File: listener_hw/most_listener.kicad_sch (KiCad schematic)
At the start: 121 parts, among them J1 1-1394640-1, J2 ANALYSER, J3 I2S, J4 VBAT_IN, J5 PLR135/T10, J6 PLT133/T10W, J7 RCA 75R, M1 Tang Nano 20K, M2 ESP32-DevKitC-VIE, U1 74LVC1G34, U10 TPS2553DBVR, U11 74LVC1G123, U12 DIR9001, U13 SRC4192, U14 LP5907MFX-3.3, U2 74LVC1G157, U3 74LVC1G125, U4 74LVC1G123, U5 TPS7B8133DRV, U6 LMR38020F, U7 Si514, U8 LP5907MFX-3.3, U9 74LVC1G79, X1 24.576MHz

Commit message: Board: J1's footprint from TE's drawing - the MOST pigtail FOT unit, measured off C-2-2141577-1
TE's specifications (114-18997 A3, 108-94198 B) give the pin allocation and
the mounting rules but refer to the product drawing for the layout, so the
footprint is measured off the customer view model drawing the user supplied:
2:1 views, the front view (contacts down) for the x positions, the side view
for the depths. Eight 0.5 mm pins in one row on 2.54 with 3.86 between pins
4 and 5 (TX 1..4 data, GND, VCC, CONT; RX 5..8 VCC, GND, MODEout, Vout), two
2.0 mm standoffs, two 0.4 mm action pins in 1.8 mm plated holes (pad 0, the
symbol's shield pin: they may be soldered), four guide legs; the optical
face 15.4 mm past the pins overhangs the board edge. Every hole equals
usb2most's TYCO_1_1394640_1 (GPLv3; that board runs on a car), which is the
cross-check. Pin 1 is at +x, as the front view's left.

Co-Authored-By: Claude Fable 5.1 <noreply@anthropic.com>
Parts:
- J1: footprint (none) -> most_listener:TE_MOST_Pigtail_FOT_2+0
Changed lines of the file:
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@@
   (property "Reference" "J1" (at 33.02 138.43 0) (effects (font (size 1.27 1.27)) (justify left bottom)))
   (property "Value" "1-1394640-1" (at 31.75 151.13 0) (effects (font (size 1.27 1.27)) (justify right)))
-  (property "Footprint" "" (at 45.72 151.13 0) (effects (font (size 1.27 1.27)) (hide yes)))
+  (property "Footprint" "most_listener:TE_MOST_Pigtail_FOT_2+0" (at 45.72 151.13 0) (effects (font (size 1.27 1.27)) (hide yes)))
   (property "Datasheet" "" (at 45.72 151.13 0) (effects (font (size 1.27 1.27)) (hide yes)))
   (pin "5") (pin "3") (pin "4") (pin "8") (pin "7") (pin "1") (pin "6") (pin "2") (pin "0")

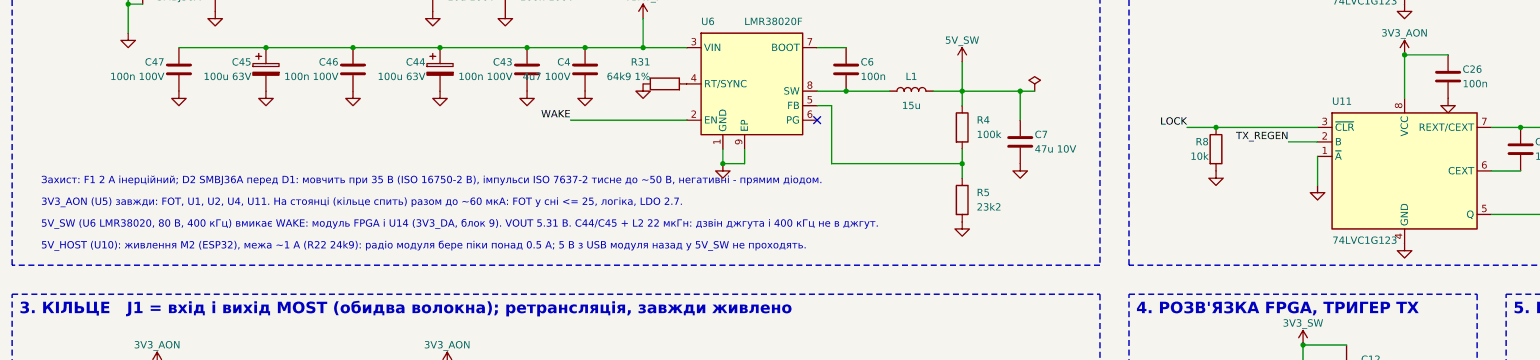
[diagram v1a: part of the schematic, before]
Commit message: Board: PCB placed - gen_listener_pcb.py lays out 130 x 90 mm from the sheet; J4 Molex Micro-Fit; J1's rear silk broken around the guide legs
listener_hw/gen_listener_pcb.py (run with KiCad's own Python, which carries
pcbnew) takes the netlist kicad-cli exports from most_listener.kicad_sch,
loads the footprints from most_listener.pretty and KiCad's libraries, places
every part at the (x, y, rotation) PLACE names - the docstring says what
sits where and why - and writes most_listener.kicad_pcb: two layers, the
outline, four M3 holes, GND pours on both sides, a copper keep-out under
M2's PCB antenna, the net classes (Default 0.25 mm / 0.15 clearance, Power
0.6 mm) into most_listener.kicad_pro, and work/most_listener.dsn, the
Specctra export for the autorouter. The file is canonical: KiCad orders the
items by uuids it draws afresh each run, so the blocks are sorted by content
and the uuids numbered; two runs give the same file, and check_all.py now
checks that the generators reproduce the committed files. DRC
(--severity-all): no error; the ten warnings are the silk of the flush
connectors J1 J5 J6 J7 M2 clipped by the edge; 313 unconnected items - the
copper is not routed yet.

Placement in short: J1 at the left edge, its face 3.6 mm past it, the FOT
cluster between its pins and M1's ring pins, the Si514 under CLK_1024; M1 in
the middle (the board under the module stays routable); M2 at the right with
the USB at the edge; block 9 along the top edge, DIR9001 turned to face J5,
X1 and U14 between J6 and J7; the battery input, the buck and J3 along the
bottom; U10 under M2's 5 V pin, J2 on the right edge.

J4 is Molex Micro-Fit 3.0 43045-0212 (2 pins, vertical, latched, 5 A)
instead of JST XH: a harness connector with a latch. J1's rear silk line ran
through the two guide-leg holes; it is drawn in three pieces now.
gen_listener.py leaves an existing most_listener.kicad_pro alone (the board
generator fills it). check_all.py: board generate, DRC (errors read from the
JSON r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
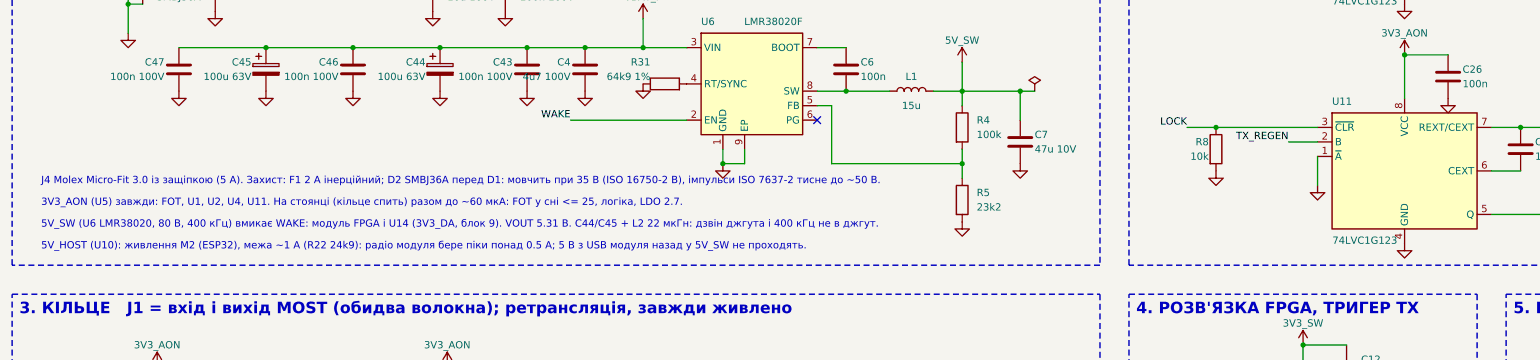
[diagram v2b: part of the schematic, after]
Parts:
- J4: footprint Connector_JST:JST_XH_B2B-XH-A_1x02_P2.50mm_Vertical -> Connector_Molex:Molex_Micro-Fit_3.0_43045-0212_2x01_P3.00mm_Vertical
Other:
- note added: "J4 Molex Micro-Fit 3.0 із защіпкою (5 А). Захист: F1 2 А інерційний; D2 SMBJ36A перед D1: мовчить при 35 В (ISO 16750-2 B), імпульси ISO 7637-2 тисне до ~50 В."
- note removed: "Захист: F1 2 А інерційний; D2 SMBJ36A перед D1: мовчить при 35 В (ISO 16750-2 B), імпульси ISO 7637-2 тисне до ~50 В, негативні - прямим діодом."
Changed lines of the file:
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@@
   (property "Reference" "J4" (at 21.59 40.64 0) (effects (font (size 1.27 1.27)) (justify left bottom)))
   (property "Value" "VBAT_IN" (at 21.59 50.8 0) (effects (font (size 1.27 1.27)) (justify left top)))
-  (property "Footprint" "Connector_JST:JST_XH_B2B-XH-A_1x02_P2.50mm_Vertical" (at 25.4 45.72 0) (effects (font (size 1.27 1.27)) (hide yes)))
+  (property "Footprint" "Connector_Molex:Molex_Micro-Fit_3.0_43045-0212_2x01_P3.00mm_Vertical" (at 25.4 45.72 0) (effects (font (size 1.27 1.27)) (hide yes)))
   (property "Datasheet" "" (at 25.4 45.72 0) (effects (font (size 1.27 1.27)) (hide yes)))
   (pin "1") (pin "2")
@@
   (pin "1")
   (instances (project "most_listener" (path "/1dba4ab3-cb1b-59ba-ab72-d256b8063c7a" (reference "#PWR007") (unit 1)))))
-(text "Захист: F1 2 А інерційний; D2 SMBJ36A перед D1: мовчить при 35 В (ISO 16750-2 B), імпульси ISO 7637-2 тисне до ~50 В, негативні - прямим діодом." (exclude_from_sim no) (at 17.78 87.63 0) (effects (font (size 1.27 1.27)) (justify left bottom)))
+(text "J4 Molex Micro-Fit 3.0 із защіпкою (5 А). Захист: F1 2 А інерційний; D2 SMBJ36A перед D1: мовчить при 35 В (ISO 16750-2 B), імпульси ISO 7637-2 тисне до ~50 В." (exclude_from_sim no) (at 17.78 87.63 0) (effects (font (size 1.27 1.27)) (justify left bottom)))
 (text "3V3_AON (U5) завжди: FOT, U1, U2, U4, U11. На стоянці (кільце спить) разом до ~60 мкА: FOT у сні <= 25, логіка, LDO 2.7." (exclude_from_sim no) (at 17.78 91.44 0) (effects (font (size 1.27 1.27)) (justify left bottom)))
 (text "5V_SW (U6 LMR38020, 80 В, 400 кГц) вмикає WAKE: модуль FPGA і U14 (3V3_DA, блок 9). VOUT 5.31 В. C44/C45 + L2 22 мкГн: дзвін джгута і 400 кГц не в джгут." (exclude_from_sim no) (at 17.78 95.25 0) (effects (font (size 1.27 1.27)) (justify left bottom)))

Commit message: Board: routed - FreeRouting session imported by the generator; J4 a right-angle Micro-Fit on the left edge; U14 in the corridor; Rail net class
most_listener.ses is FreeRouting 2.4.1's session for the exported placement
(-mp 100 -mt 1, about four minutes); gen_listener_pcb.py imports it when it
lies beside the sheet, lays the top ground pour over the tracks, fills both
pours and saves - so the routed board, too, is reproduced from the committed
files (check_all.py now diffs the .kicad_pcb and the generated .kicad_dru as
well). DRC: no error, no unconnected item; the twelve warnings are the flush
connectors' silk clipped by the board edge.

What it took: the Specctra export carries only the bottom pour. With pours
on both sides the router left GND pads on scraps of the top pour between
foreign tracks, with no room for a via (a stub-and-via stitching pass was
tried and dropped); with the bottom plane alone it escapes every GND pad to
it by a via, and the top pour laid afterwards just adds copper. The sheet's
unconnected-* nets get no net on the board (U7 has three pad-5 copies in
one such net and the router tried to join them). The 3.3 V rails moved from
Power to a Rail class of 0.35 mm - tens of milliamps, and 0.6 mm does not
pass between a module's pins. U14 (block 9's LDO) sits in the corridor under
D3, where 5V_SW arrives from below without crossing block 9; R20/R21 sit
under M2's IO25/IO27 pins; R6 and C9 at U4's right column, where the pins
they serve are. most_listener.kicad_dru asks for one resolved thermal spoke
instead of two.

J4 is now Molex Micro-Fit 3.0 43650-0200, right-angle, flush on the left
edge under J1 (mating housing 43645-0200, terminals 43030): the car's two
cables, fibre and power, leave through one face and the audio through the
top. The user asked whether the power connector could join the others on one
side; everything on the top edge would have dragged the battery input next
to the Si514 and the FOT cluster.

Co-Authored-By: Claude Fable 5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
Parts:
- J4: footprint Connector_Molex:Molex_Micro-Fit_3.0_43045-0212_2x01_P3.00mm_Vertical -> Connector_Molex:Molex_Micro-Fit_3.0_43650-0200_1x02_P3.00mm_Horizontal
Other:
- note added: "J4 Molex Micro-Fit 3.0 кутовий 43650-0200 на лівому краю під J1 (відповідна частина 43645-0200, контакти 43030), із защіпкою, 5 А. Захист: F1 2 А інерційний; D2 SMBJ36A перед D1: мовчить при 35 В (ISO 16750-2 B), імпульси ISO 7637-2 тисне до ~50 В."
- note removed: "J4 Molex Micro-Fit 3.0 із защіпкою (5 А). Захист: F1 2 А інерційний; D2 SMBJ36A перед D1: мовчить при 35 В (ISO 16750-2 B), імпульси ISO 7637-2 тисне до ~50 В."
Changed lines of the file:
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@@
   (property "Reference" "J4" (at 21.59 40.64 0) (effects (font (size 1.27 1.27)) (justify left bottom)))
   (property "Value" "VBAT_IN" (at 21.59 50.8 0) (effects (font (size 1.27 1.27)) (justify left top)))
-  (property "Footprint" "Connector_Molex:Molex_Micro-Fit_3.0_43045-0212_2x01_P3.00mm_Vertical" (at 25.4 45.72 0) (effects (font (size 1.27 1.27)) (hide yes)))
+  (property "Footprint" "Connector_Molex:Molex_Micro-Fit_3.0_43650-0200_1x02_P3.00mm_Horizontal" (at 25.4 45.72 0) (effects (font (size 1.27 1.27)) (hide yes)))
   (property "Datasheet" "" (at 25.4 45.72 0) (effects (font (size 1.27 1.27)) (hide yes)))
   (pin "1") (pin "2")
@@
   (pin "1")
   (instances (project "most_listener" (path "/1dba4ab3-cb1b-59ba-ab72-d256b8063c7a" (reference "#PWR007") (unit 1)))))
-(text "J4 Molex Micro-Fit 3.0 із защіпкою (5 А). Захист: F1 2 А інерційний; D2 SMBJ36A перед D1: мовчить при 35 В (ISO 16750-2 B), імпульси ISO 7637-2 тисне до ~50 В." (exclude_from_sim no) (at 17.78 87.63 0) (effects (font (size 1.27 1.27)) (justify left bottom)))
+(text "J4 Molex Micro-Fit 3.0 кутовий 43650-0200 на лівому краю під J1 (відповідна частина 43645-0200, контакти 43030), із защіпкою, 5 А. Захист: F1 2 А інерційний; D2 SMBJ36A перед D1: мовчить при 35 В (ISO 16750-2 B), імпульси ISO 7637-2 тисне до ~50 В." (exclude_from_sim no) (at 17.78 87.63 0) (effects (font (size 1.27 1.27)) (justify left bottom)))
 (text "3V3_AON (U5) завжди: FOT, U1, U2, U4, U11. На стоянці (кільце спить) разом до ~60 мкА: FOT у сні <= 25, логіка, LDO 2.7." (exclude_from_sim no) (at 17.78 91.44 0) (effects (font (size 1.27 1.27)) (justify left bottom)))
 (text "5V_SW (U6 LMR38020, 80 В, 400 кГц) вмикає WAKE: модуль FPGA і U14 (3V3_DA, блок 9). VOUT 5.31 В. C44/C45 + L2 22 мкГн: дзвін джгута і 400 кГц не в джгут." (exclude_from_sim no) (at 17.78 95.25 0) (effects (font (size 1.27 1.27)) (justify left bottom)))
